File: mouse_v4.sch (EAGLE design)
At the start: 71 parts, among them U2 DRV8835DSSR

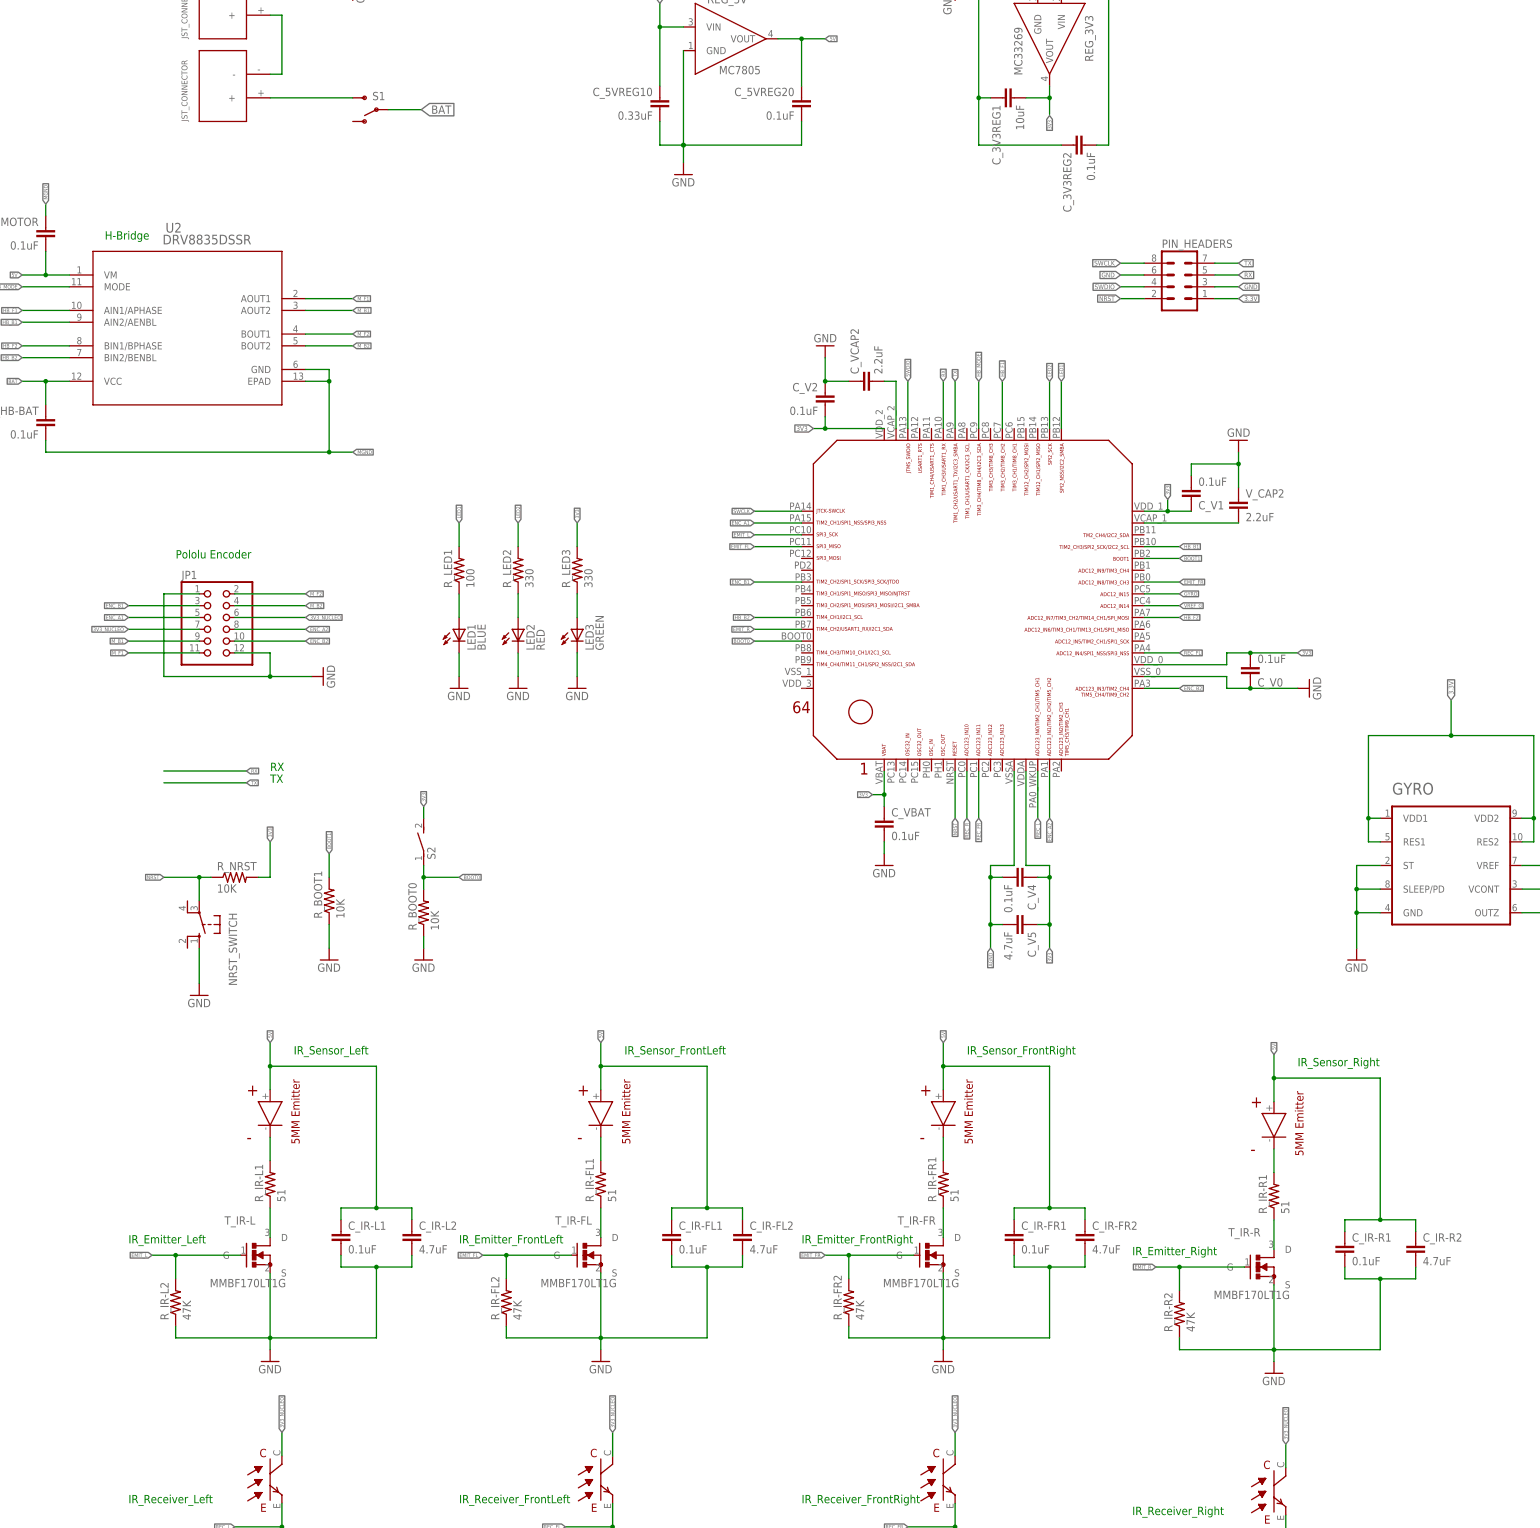
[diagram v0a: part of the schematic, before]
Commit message: v4 pre-polygon
Moved H-Bridge closer
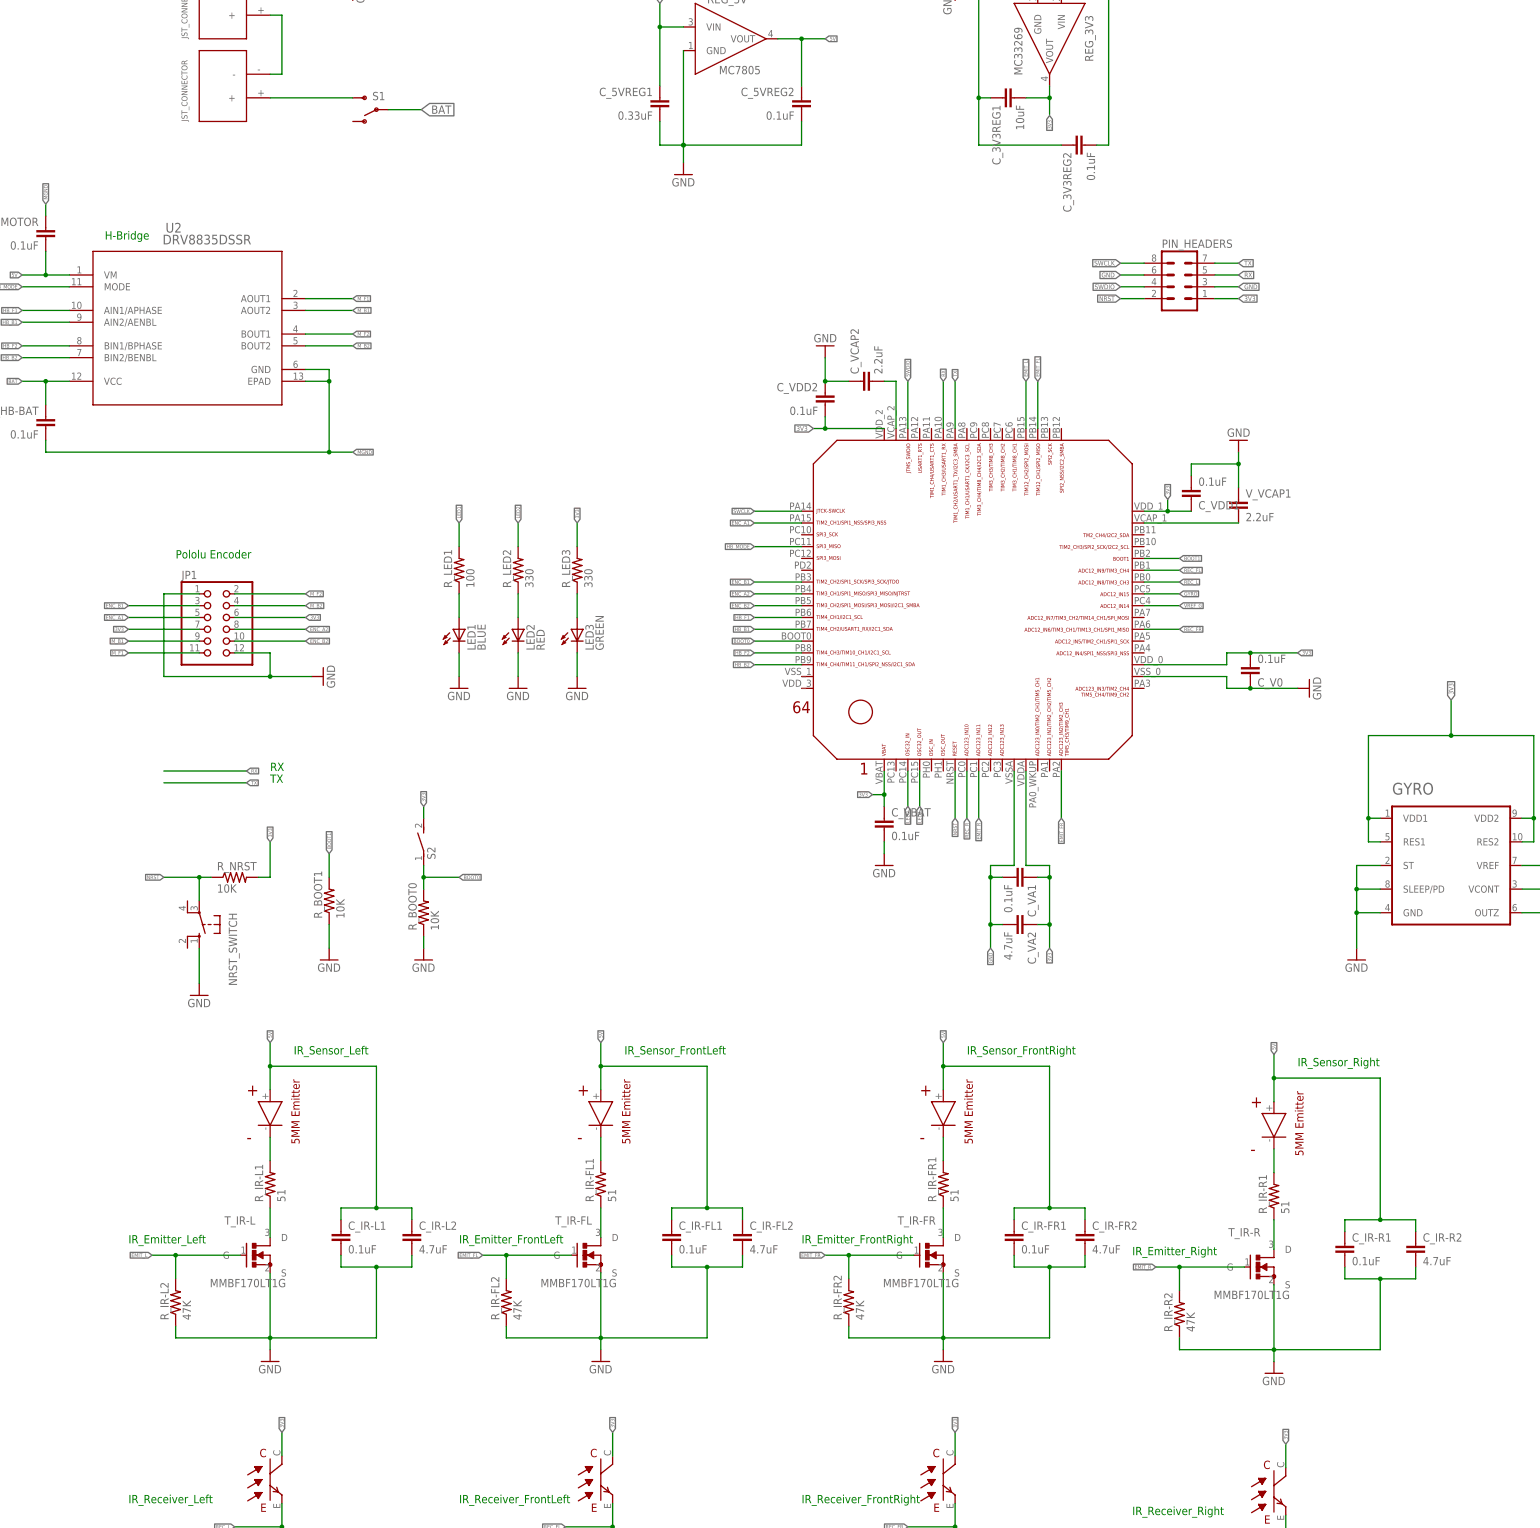
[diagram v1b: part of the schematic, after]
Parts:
- R_BOOT0, R_BOOT1, R_NRST: device rcl:R-US_0204/2V -> SparkFun-Resistors:1.8KOHM1/10W1%(0603)
- renumbered C_5VREG10 to C_5VREG1, C_5VREG20 to C_5VREG2, C_V1 to C_VDD1, C_V2 to C_VDD2, C_V4 to C_VA1, C_V5 to C_VA2, V_CAP2 to V_VCAP1
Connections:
- removed net 3.3V: GYRO.RES1, GYRO.RES2, GYRO.VDD1, GYRO.VDD2, PIN_HEADERS.1
- removed net 3V3_NUCLEO: JP1.6, JP1.7, U$4.C, U$5.C, U$6.C, U$7.C
- removed net AGND: C_VA1.2, C_VA2.2, U$1.VSSA
- removed net N$1: R_BOOT1.1
- net 3V3: now also GYRO.RES1, GYRO.RES2, GYRO.VDD1, GYRO.VDD2, JP1.6, JP1.7, PIN_HEADERS.1, U$4.C, U$5.C, U$6.C, U$7.C
- net EMIT_FL: now also U$1.PB14; no longer U$1.PC11
- net EMIT_FR: now also U$1.PA2; no longer U$1.PB0
- net EMIT_L: now also U$1.PB15; no longer U$1.PC10
- net EMIT_R: now also U$1.PC1; no longer U$1.PB7
- net ENC_A2: now also U$1.PB4; no longer U$1.PA1
- net ENC_B2: now also U$1.PB5; no longer U$1.PA3
- net GND: now also C_VA1.2, C_VA2.2, R_BOOT1.1, U$1.VSSA
- net HB_B1: now also U$1.PB7; no longer U$1.PB10
- net HB_B2: now also U$1.PB9; no longer U$1.PB6
- net HB_F1: now also U$1.PB6; no longer U$1.PC7
- net HB_F2: now also U$1.PB8; no longer U$1.PA7
- net HB_MODE: now also U$1.PC11; no longer U$1.PC9
- net LED1: now also U$1.PC15; no longer U$1.PB12
- net LED2: now also U$1.PC14; no longer U$1.PB13
- net REC_FL: now also U$1.PB1; no longer U$1.PA4
- net REC_FR: now also U$1.PA6; no longer U$1.PC1
- net REC_L: now also U$1.PB0; no longer U$1.PA0_AKUP
